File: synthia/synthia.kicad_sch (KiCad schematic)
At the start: 90 parts, among them J1 MJ-63022B, J2 SJ3-35083C-TR, J3 PJ-007, J4 SDS-50J, Q1 IRF9540N, U1 TLV272IP, U2 STM32H750ZBT6, U3 LD1117V33, U4 PVA1EEH31.2NV2, U5 PVA1EEH31.2NV2

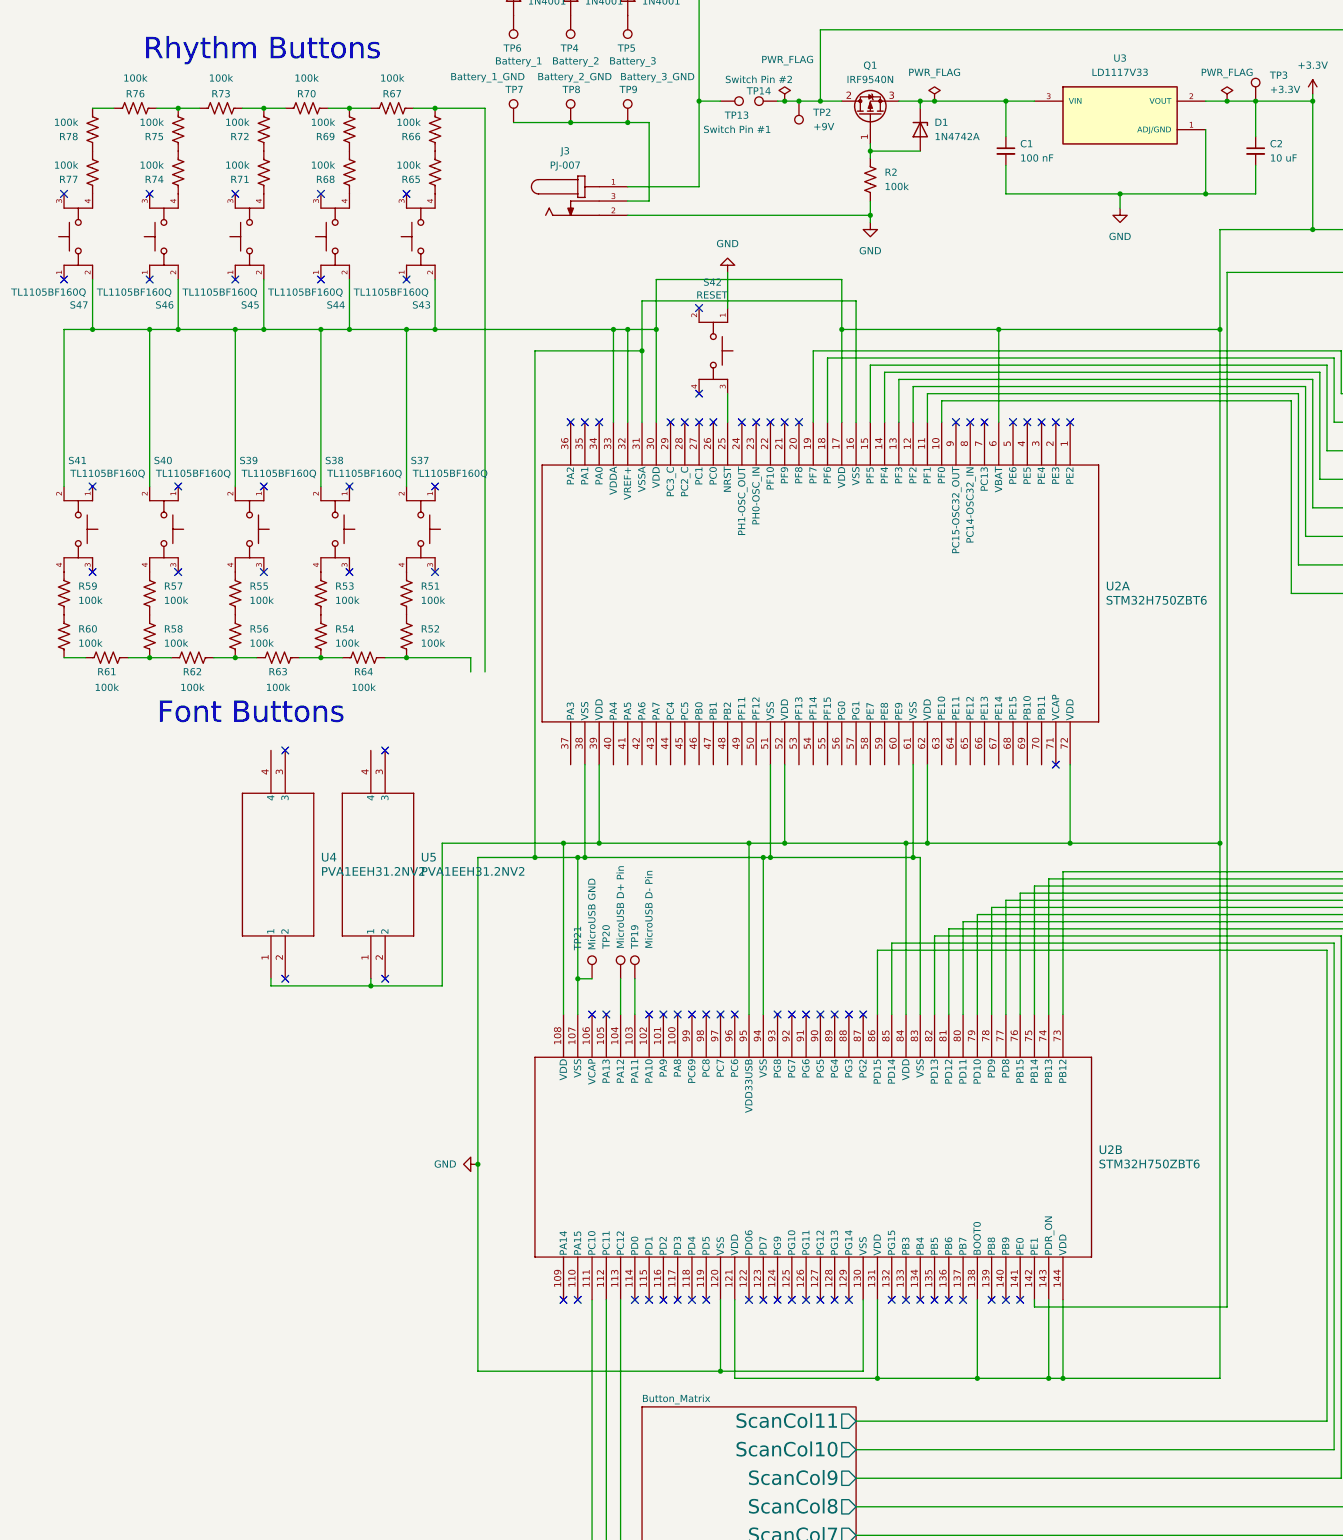
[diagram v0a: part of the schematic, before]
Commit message: Completely had to redesign most of the pins allocated for power and designed some of the ports that will save us from potentially bricking the stm. PCB wiring for the updated schematic is NOT DONE
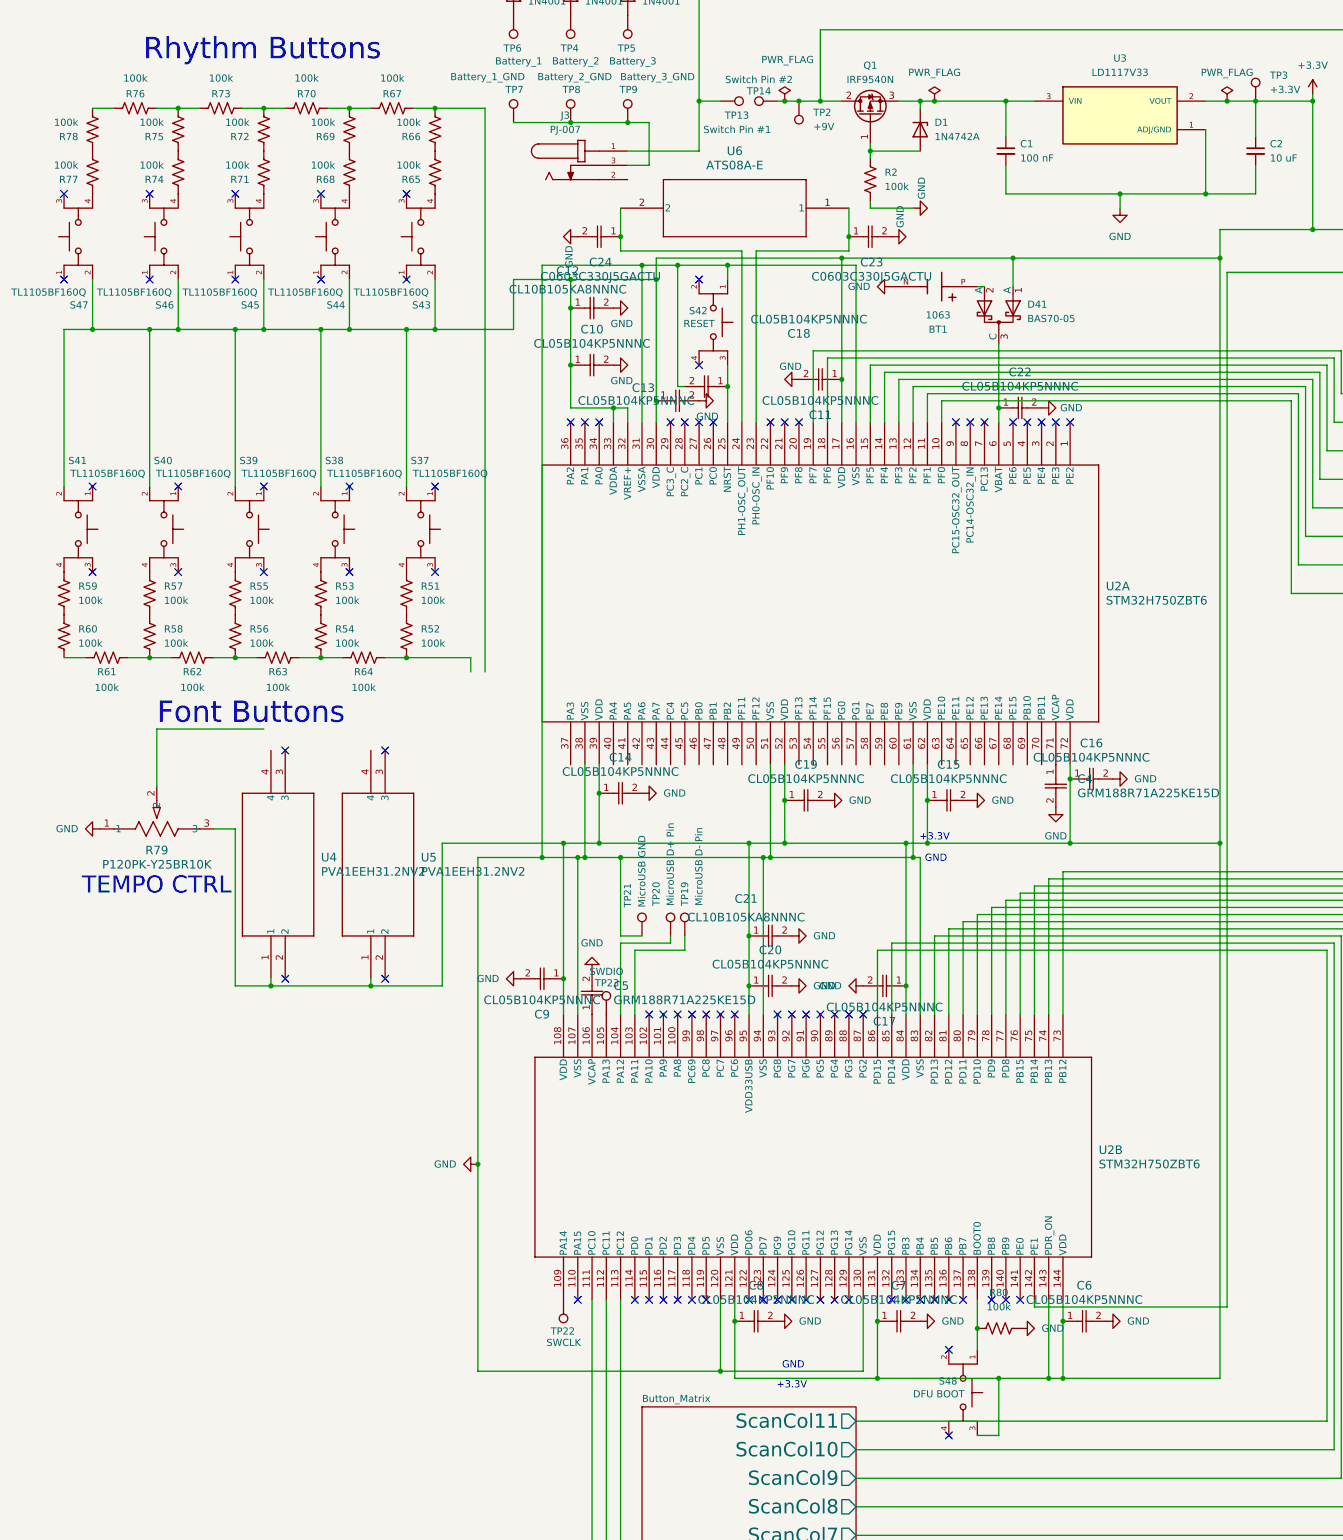
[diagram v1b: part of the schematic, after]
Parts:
- added BT1: 1063, Synthia_footprint_library:BAT_1063, symbol Synthia_Symbol_Library:1063
- added C10, C11, C13, C14, C15, C16, C17, C18, C19, C20, C22, C6, C7, C8, C9: CL05B104KP5NNNC, Synthia_footprint_library:CAP_CL05_SAM-L, symbol Synthia_Symbol_Library:CL05B104KP5NNNC
- added C12, C21: CL10B105KA8NNNC, Synthia_footprint_library:CAP_CL10_SAM-L, symbol Synthia_Symbol_Library:CL10B105KA8NNNC
- added C23, C24: C0603C330J5GACTU, Synthia_footprint_library:CAPC17595_87N_KEM-L, symbol Synthia_Symbol_Library:C0603C330J5GACTU
- added C4, C5: GRM188R71A225KE15D, Synthia_footprint_library:G-188_MUR, symbol Synthia_Symbol_Library:GRM188R71A225KE15D
- added D41: BAS70-05, Synthia_footprint_library:P200_SOT-23, symbol Synthia_Symbol_Library:BAS70-05
- added R79: P120PK-Y25BR10K, Synthia_footprint_library:POT_P120PK-x25_TTE, symbol Synthia_Symbol_Library:P120PK-Y25BR10K
- added R80: 100k, Synthia_footprint_library:STA_CF14_STP, symbol Device:R_US
- added S48: DFU BOOT, Synthia_footprint_library:SW_TL1105BF160Q, symbol Synthia_Symbol_Library:TL1105BF160Q
- added TP22: SWCLK, TestPoint:TestPoint_Plated_Hole_D2.0mm, symbol Connector:TestPoint
- added TP23: SWDIO, TestPoint:TestPoint_Plated_Hole_D2.0mm, symbol Connector:TestPoint
- added U6: ATS08A-E, Synthia_footprint_library:ATS08A-E_CTS, symbol Synthia_Symbol_Library:ATS08A-E
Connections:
- net +3.3V: now also C10.1, C11.1, C12.1, C13.1, C14.1, C15.1, C16.1, C17.1, C19.1, C20.1, C21.1, C6.1, C7.1, C8.1, C9.1, D41.1 (A), R79.3, S48.3; no longer U2.138 (BOOT0), U2.6 (VBAT)
- net GND: now also BT1.N, C10.2, C11.2, C12.2, C13.2, C14.2, C15.2, C16.2, C17.2, C18.2, C19.2, C20.2, C21.2, C22.2, C23.2, C24.2, C4.2, C5.2, C6.2, C7.2, C8.2, C9.2, R79.1, R80.2; no longer J3.2
- net at S42.3, U2.25 (NRST): now also C18.1
- net at U2.23 (PH0-OSC_IN): now also C23.1, U6.1
- net at U2.24 (PH1-OSC_OUT): now also C24.1, U6.2
- net at U2.71 (VCAP): now also C4.1
- net at U2.105 (PA13): now also TP23.1
- net at U2.106 (VCAP): now also C5.1
- net at U2.109 (PA14): now also TP22.1
- new net: BT1.P, D41.2 (A)
- new net: C22.1, D41.3 (C), U2.6 (VBAT)
- new net: R80.1, S48.1, U2.138 (BOOT0)
- no-connect marks 90 -> 86
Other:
- note added: "+3.3V"
- note added: "GND"
- note added: "TEMPO CTRL"
- moved on the sheet: J3, S42, TP19, TP20, TP21

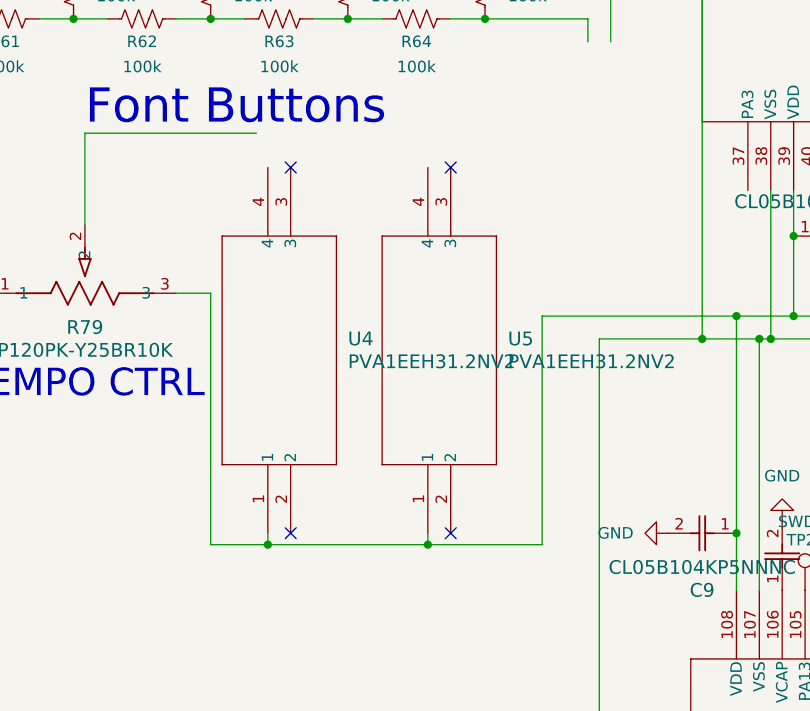
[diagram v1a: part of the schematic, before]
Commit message: Organized Font and Rhythm button matrices and associated switches. Not in their final location so power and IO is not routed for them yet
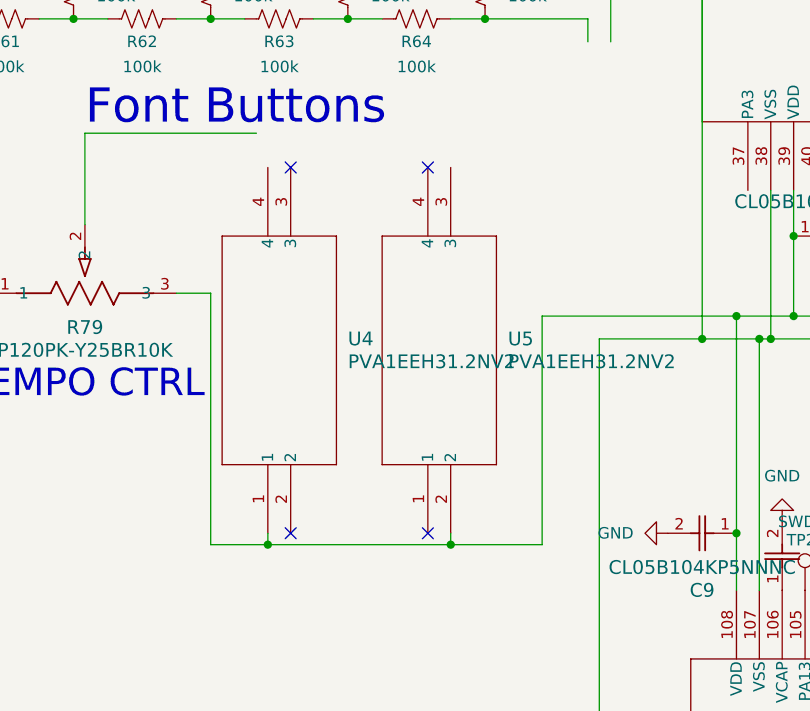
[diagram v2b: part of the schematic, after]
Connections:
- net +3.3V: now also U5.2; no longer U5.1
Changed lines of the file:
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@@
 	)
 	(junction
-		(at 71.12 200.66)
+		(at 73.66 200.66)
 		(diameter 0)
 		(color 0 0 0 0)
@@
 	)
 	(no_connect
-		(at 73.66 158.75)
-	)
-	(no_connect
 		(at 67.31 111.76)
 	)
@@
 	)
 	(no_connect
+		(at 71.12 158.75)
+	)
+	(no_connect
 		(at 111.76 100.33)
 	)
@@
 	)
 	(no_connect
-		(at 73.66 199.39)
-	)
-	(no_connect
 		(at 184.15 256.54)
 	)
@@
 	)
 	(no_connect
+		(at 71.12 199.39)
+	)
+	(no_connect
 		(at 16.51 74.93)
 	)
@@
 	(wire
 		(pts
-			(xy 71.12 200.66) (xy 83.82 200.66)
-		)
-		(stroke
-			(width 0)
-			(type default)
-		)
-	)
-	(wire
-		(pts
 			(xy 83.82 175.26) (xy 83.82 200.66)
 		)
@@
 	(wire
 		(pts
-			(xy 71.12 199.39) (xy 71.12 200.66)
-		)
-		(stroke
-			(width 0)
-			(type default)
-		)
-	)
-	(wire
-		(pts
 			(xy 160.02 62.23) (xy 160.02 60.96)
 		)
@@
 	(wire
 		(pts
-			(xy 53.34 200.66) (xy 71.12 200.66)
+			(xy 53.34 200.66) (xy 73.66 200.66)
 		)
 		(stroke
@@
 	(wire
 		(pts
+			(xy 73.66 199.39) (xy 73.66 200.66)
+		)
+		(stroke
+			(width 0)
+			(type default)
+		)
+	)
+	(wire
+		(pts
 			(xy 121.92 71.12) (xy 121.92 74.93)
 		)
@@
 		)
 		(stroke
+			(width 0)
+			(type default)
+		)
+	)
+	(wire
+		(pts
+			(xy 73.66 200.66) (xy 83.82 200.66)
+		)
+		(stroke
